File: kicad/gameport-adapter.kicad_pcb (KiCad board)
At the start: 2 copper layers, 45.7 x 39.4 mm, 8 parts, among them SW1 SW_DIP_x04, U1 Arduino_Pro_Micro

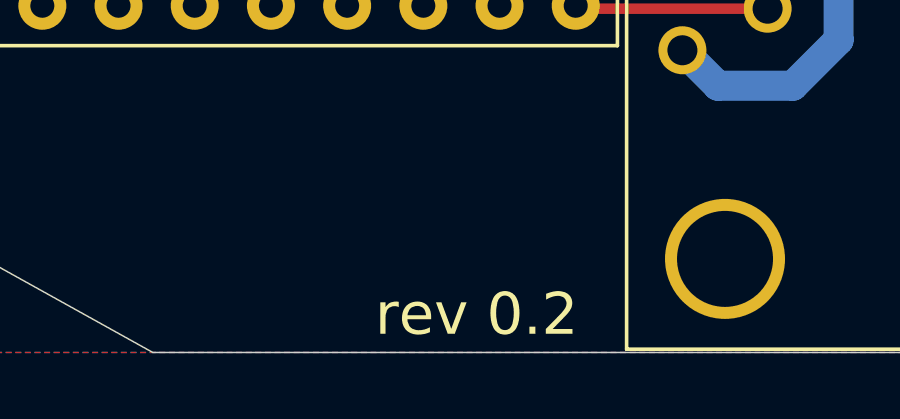
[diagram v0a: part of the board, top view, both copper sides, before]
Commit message: Minor silk layer fixes, rev 0.2.1
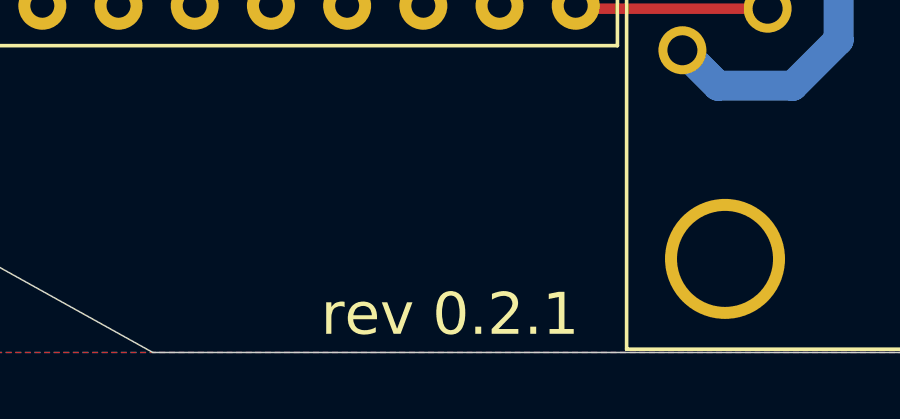
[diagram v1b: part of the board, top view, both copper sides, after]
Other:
- board text added: "https://github.com/necroware"
- board text added: "rev 0.2.1"
- board text removed: "rev 0.2"
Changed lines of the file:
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@@
-(kicad_pcb (version 20171130) (host pcbnew 5.1.9)
+(kicad_pcb (version 20171130) (host pcbnew 5.1.12)
   (general
     (thickness 1.6)
-    (drawings 12)
+    (drawings 13)
     (tracks 61)
     (zones 0)
@@
   (title_block
     (title "GamePort Adapter")
-    (date 2021-04-01)
-    (rev 0.2)
+    (date 2022-01-07)
+    (rev 0.2.1)
     (company Necroware)
     (comment 1 "by Scorp")
@@
     (44 Edge.Cuts user)
     (45 Margin user)
-    (46 B.CrtYd user hide)
-    (47 F.CrtYd user hide)
+    (46 B.CrtYd user)
+    (47 F.CrtYd user)
     (48 B.Fab user)
-    (49 F.Fab user hide)
+    (49 F.Fab user)
   )
   (setup
@@
     (add_net MIDI_RXD)
     (add_net MIDI_TXD)
-    (add_net "Net-(U1-Pad1)")
-    (add_net "Net-(U1-Pad2)")
-    (add_net "Net-(U1-Pad22)")
-    (add_net "Net-(U1-Pad24)")
-    (add_net "Net-(U1-Pad5)")
-    (add_net "Net-(U1-Pad6)")
     (add_net SW1)
     (add_net SW2)
@@
     )
   )
-  (gr_text 15 (at 114.3 98.425 90) (layer B.Paste)
+  (gr_text https://github.com/necroware (at 119.888 88.138 90) (layer B.SilkS)
+    (effects (font (size 1.5 1.4) (thickness 0.275)) (justify mirror))
+  )
+  (gr_text 15 (at 114.3 98.425 90) (layer B.SilkS)
     (effects (font (size 1 1) (thickness 0.15)) (justify mirror))
   )
-  (gr_text 9 (at 114.3 78.105 90) (layer B.Paste)
+  (gr_text 9 (at 114.3 78.105 90) (layer B.SilkS)
     (effects (font (size 1 1) (thickness 0.15)) (justify mirror))
   )
-  (gr_text 8 (at 111.76 99.695 90) (layer B.Paste)
+  (gr_text 8 (at 111.76 99.695 90) (layer B.SilkS)
     (effects (font (size 1 1) (thickness 0.15)) (justify mirror))
   )
-  (gr_text 1 (at 111.76 76.835 90) (layer B.Paste)
+  (gr_text 1 (at 111.76 76.835 90) (layer B.SilkS)
     (effects (font (size 1 1) (thickness 0.15)) (justify mirror))
   )
-  (gr_text "rev 0.2" (at 104.775 106.68) (layer F.SilkS)
+  (gr_text "rev 0.2.1" (at 103.886 106.68) (layer F.SilkS)
     (effects (font (size 1.4 1.4) (thickness 0.2)))
   )

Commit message: Upgrade project to KiCad 6.x
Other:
- net class Default removed
- net class Power removed
